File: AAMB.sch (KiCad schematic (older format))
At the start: 6 parts, among them J1 Screw_Terminal_01x04, J2 PJRAS4X2U01X, J3 SPKR L, J4 SPKR R, J5 Screw_Terminal_01x03

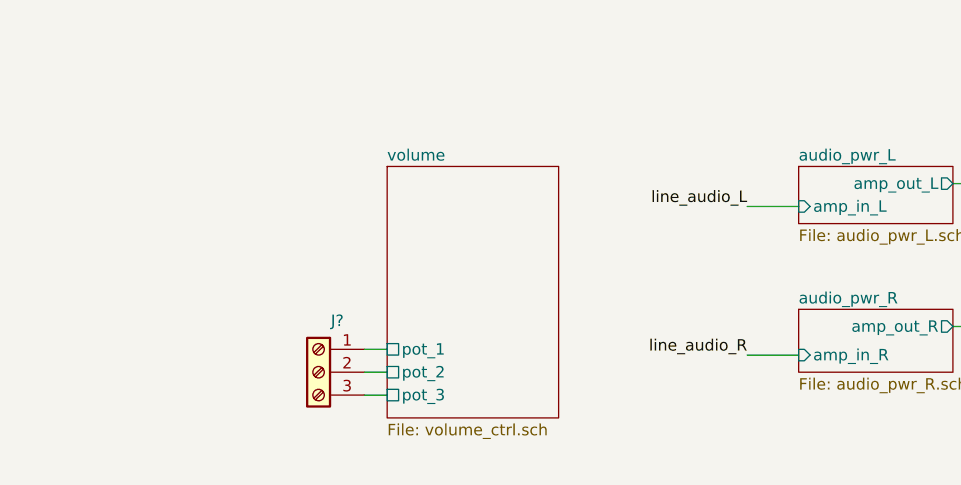
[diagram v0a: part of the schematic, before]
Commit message: Volume circuit placed and connected. Page titles added.
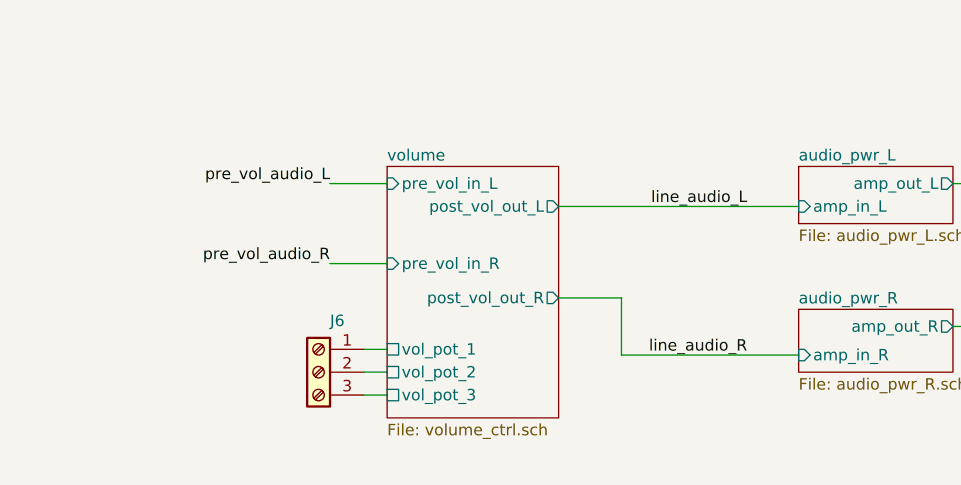
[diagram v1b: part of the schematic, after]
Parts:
- gave numbers to parts that had none: 1
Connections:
- net labels added: pre_vol_audio_L, pre_vol_audio_R
- wire segments 37 -> 41
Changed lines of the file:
@@
 encoding utf-8
 Sheet 1 5
-Title ""
-Date ""
-Rev ""
-Comp ""
-Comment1 ""
-Comment2 ""
+Title "Audio Amp Main Board Top"
+Date "2020-01-21"
+Rev "A"
+Comp "Shawn Adams"
+Comment1 "Based on designs by Elliot Sound Products"
+Comment2 "https://sound-au.com/"
 Comment3 ""
 Comment4 ""
@@
 Wire Wire Line
 	900  1550 1100 1550
-Wire Wire Line
-	6925 4275 7150 4275
 NoConn ~ 1050 4925
 NoConn ~ 1050 4425
@@
 line_audio_R
 Wire Wire Line
-	7150 4925 6925 4925
-Wire Wire Line
 	8450 4325 8450 4800
 Text Label 7950 4800 0    50   ~ 0
@@
 	7825 4800 8450 4800
 $Comp
-L Connector:Screw_Terminal_01x03 J?
+L Connector:Screw_Terminal_01x03 J6
 U 1 1 5E22654E
 P 5050 5000
-F 0 "J?" H 4968 5225 50  0000 C CNN
+F 0 "J6" H 4968 5225 50  0000 C CNN
 F 1 "Screw_Terminal_01x03" H 4968 5226 50  0001 C CNN
 F 2 "" H 5050 5000 50  0001 C CNN
@@
 F0 "volume" 50
 F1 "volume_ctrl.sch" 50
-F2 "pot_1" U L 5350 4900 50
-F3 "pot_2" U L 5350 5000 50
-F4 "pot_3" U L 5350 5100 50
+F2 "vol_pot_1" U L 5350 4900 50
+F3 "vol_pot_2" U L 5350 5000 50
+F4 "vol_pot_3" U L 5350 5100 50
+F5 "post_vol_out_L" O R 6100 4275 50
+F6 "pre_vol_in_L" I L 5350 4175 50
+F7 "pre_vol_in_R" I L 5350 4525 50
+F8 "post_vol_out_R" O R 6100 4675 50
 $EndSheet
 Wire Wire Line
@@
 EndData
 $EndBitmap
+Wire Wire Line
+	6100 4675 6375 4675
+Wire Wire Line
+	6375 4675 6375 4925
+Wire Wire Line
+	6375 4925 7150 4925
+Wire Wire Line
+	6100 4275 7150 4275
+Wire Wire Line
+	5350 4175 5100 4175
+Wire Wire Line
+	5350 4525 5100 4525
+Text Label 5100 4175 2    50   ~ 0
+pre_vol_audio_L
+Text Label 5100 4525 2    50   ~ 0
+pre_vol_audio_R
 $EndSCHEMATC

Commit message: Started input select circuit.
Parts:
- added J?: Conn_01x05, symbol Connector_Generic:Conn_01x05
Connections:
- net labels removed: IN1_L, IN1_R, IN2_L, IN2_R, IN3_L, IN3_R, IN4_L, IN4_R
- wire segments 41 -> 60
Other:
- note added: "volume knob\n10k linear pot"
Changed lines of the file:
@@
 $Descr A4 11693 8268
 encoding utf-8
-Sheet 1 5
+Sheet 1 6
 Title "Audio Amp Main Board Top"
 Date "2020-01-21"
 Rev "A"
 Comp "Shawn Adams"
-Comment1 "Based on designs by Elliot Sound Products"
-Comment2 "https://sound-au.com/"
+Comment1 "https://sound-au.com/"
+Comment2 "Based on designs by Elliot Sound Products"
 Comment3 ""
 Comment4 ""
@@
 Wire Wire Line
 	925  1800 925  1650
-Text Label 1150 3275 0    50   ~ 0
-IN1_R
-Text Label 1150 3075 0    50   ~ 0
-IN1_L
 Text Label 6925 4275 2    50   ~ 0
 line_audio_L
@@
 	1    0    0    -1
 $EndComp
-Wire Wire Line
-	1050 3775 1150 3775
-Text Label 1150 3775 0    50   ~ 0
-IN2_R
-Text Label 1150 3575 0    50   ~ 0
-IN2_L
-Wire Wire Line
-	1050 4075 1150 4075
-Wire Wire Line
-	1050 4275 1150 4275
-Text Label 1150 4275 0    50   ~ 0
-IN3_R
-Text Label 1150 4075 0    50   ~ 0
-IN3_L
-Wire Wire Line
-	1050 4575 1150 4575
-Wire Wire Line
-	1050 4775 1150 4775
-Text Label 1150 4775 0    50   ~ 0
-IN4_R
-Text Label 1150 4575 0    50   ~ 0
-IN4_L
 $Comp
 L power:GND #PWR01
@@
 	850  625  725  625
 Wire Wire Line
-	1150 3575 1050 3575
-Wire Wire Line
-	1150 3275 1050 3275
-Wire Wire Line
-	1150 3075 1050 3075
+	1175 3575 1050 3575
+Wire Wire Line
+	1100 3275 1050 3275
 Wire Wire Line
 	900  1450 950  1450
@@
 U 1 1 5E3F968D
 P 10000 4500
-F 0 "J3" H 10080 4492 50  0000 L CNN
-F 1 "SPKR L" H 10080 4401 50  0000 L CNN
+F 0 "J3" H 10075 4400 50  0000 L CNN
+F 1 "SPKR L" H 10075 4500 50  0000 L CNN
 F 2 "TerminalBlock_Phoenix:TerminalBlock_Phoenix_MKDS-1,5-2_1x02_P5.00mm_Horizontal" H 10000 4500 50  0001 C CNN
 F 3 "https://www.digikey.com/product-detail/en/phoenix-contact/1715022/277-1258-ND/260626" H 10000 4500 50  0001 C CNN
@@
 U 1 1 5E3FA9B2
 P 10000 4750
-F 0 "J4" H 10080 4742 50  0000 L CNN
-F 1 "SPKR R" H 10080 4651 50  0000 L CNN
+F 0 "J4" H 10075 4650 50  0000 L CNN
+F 1 "SPKR R" H 10075 4750 50  0000 L CNN
 F 2 "TerminalBlock_Phoenix:TerminalBlock_Phoenix_MKDS-1,5-2_1x02_P5.00mm_Horizontal" H 10000 4750 50  0001 C CNN
 F 3 "https://www.digikey.com/product-detail/en/phoenix-contact/1715022/277-1258-ND/260626" H 10000 4750 50  0001 C CNN
@@
 Text Label 5100 4525 2    50   ~ 0
 pre_vol_audio_R
+Text Notes 4175 5150 0    50   ~ 0
+volume knob\n10k linear pot
+$Sheet
+S 2100 2950 1175 1625
+U 5E487042
+F0 "input_select" 50
+F1 "input_select.sch" 50
+F2 "IN1_L" I L 2100 3075 50
+F3 "IN1_R" I L 2100 3175 50
+F4 "IN2_L" I L 2100 3325 50
+F5 "IN2_R" I L 2100 3425 50
+F6 "IN3_L" I L 2100 3550 50
+F7 "IN3_R" I L 2100 3650 50
+F8 "IN4_L" I L 2100 3775 50
+F9 "IN4_R" I L 2100 3875 50
+F10 "input_sw_0" I L 2100 4075 50
+F11 "input_sw_1" I L 2100 4175 50
+F12 "input_sw_2" I L 2100 4275 50
+F13 "input_sw_3" I L 2100 4375 50
+F14 "input_sw_com" O L 2100 4475 50
+F15 "post_sw_audio_L" O R 3275 3250 50
+F16 "post_sw_audio_R" O R 3275 3475 50
+$EndSheet
+$Comp
+L Connector_Generic:Conn_01x05 J?
+U 1 1 5E5AF883
+P 1800 4275
+F 0 "J?" H 1725 4000 50  0000 C CNN
+F 1 "Conn_01x05" H 1718 4601 50  0001 C CNN
+F 2 "" H 1800 4275 50  0001 C CNN
+F 3 "~" H 1800 4275 50  0001 C CNN
+	1    1800 4275
+	-1   0    0    -1
+$EndComp
+Wire Wire Line
+	2000 4075 2100 4075
+Wire Wire Line
+	2000 4175 2100 4175
+Wire Wire Line
+	2000 4275 2100 4275
+Wire Wire Line
+	2000 4375 2100 4375
+Wire Wire Line
+	2000 4475 2100 4475
+Wire Wire Line
+	1050 3075 2100 3075
+Wire Wire Line
+	2100 3175 1100 3175
+Wire Wire Line
+	1100 3175 1100 3275
+Wire Wire Line
+	1175 3575 1175 3325
+Wire Wire Line
+	1175 3325 2100 3325
+Wire Wire Line
+	1250 3775 1250 3425
+Wire Wire Line
+	1250 3425 2100 3425
+Wire Wire Line
+	1050 3775 1250 3775
+Wire Wire Line
+	1350 4075 1350 3550
+Wire Wire Line
+	1350 3550 2100 3550
+Wire Wire Line
+	1050 4075 1350 4075
+Wire Wire Line
+	1425 4275 1425 3650
+Wire Wire Line
+	1425 3650 2100 3650
+Wire Wire Line
+	1050 4275 1425 4275
+Wire Wire Line
+	1525 4575 1525 3775
+Wire Wire Line
+	1525 3775 2100 3775
+Wire Wire Line
+	1050 4575 1525 4575
+Wire Wire Line
+	1600 4775 1600 3875
+Wire Wire Line
+	1600 3875 2100 3875
+Wire Wire Line
+	1050 4775 1600 4775
 $EndSCHEMATC

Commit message: Opened on home office computer. Some rescue and lib conversion happened. Need to confirm no changes on work laptop.
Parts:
- J2: symbol Connectors-amp:PJRAS4X2U01X -> AAMB-rescue:PJRAS4X2U01X-Connectors-amp
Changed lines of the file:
@@
 EESchema Schematic File Version 4
-LIBS:AAMB-cache
 EELAYER 30 0
 EELAYER END
@@
 line_audio_L
 $Comp
-L Connectors-amp:PJRAS4X2U01X J2
+L AAMB-rescue:PJRAS4X2U01X-Connectors-amp J2
 U 1 1 5E2F4D8A
 P 900 3325
@@
 $EndComp
 $Comp
-L Connectors-amp:PJRAS4X2U01X J2
+L AAMB-rescue:PJRAS4X2U01X-Connectors-amp J2
 U 2 1 5E2F72BC
 P 900 3825
@@
 $EndComp
 $Comp
-L Connectors-amp:PJRAS4X2U01X J2
+L AAMB-rescue:PJRAS4X2U01X-Connectors-amp J2
 U 3 1 5E2F87B8
 P 900 4325
@@
 $EndComp
 $Comp
-L Connectors-amp:PJRAS4X2U01X J2
+L AAMB-rescue:PJRAS4X2U01X-Connectors-amp J2
 U 4 1 5E2FA23A
 P 900 4825
@@
 	8675 4325 8450 4325
 $Comp
-L Power-amp:+35V #PWR0106
+L AAMB-rescue:+35V-Power-amp #PWR0106
 U 1 1 5E1EC4AA
 P 1100 1550
@@
 $EndComp
 $Comp
-L Power-amp:-35V #PWR0107
+L AAMB-rescue:-35V-Power-amp #PWR0107
 U 1 1 5E1EDDCB
 P 1100 1750
@@
 $EndComp
 $Comp
-L Power-amp:+35V #PWR0112
+L AAMB-rescue:+35V-Power-amp #PWR0112
 U 1 1 5E239287
 P 725 625
@@
 $EndComp
 $Comp
-L Power-amp:-35V #PWR0113
+L AAMB-rescue:-35V-Power-amp #PWR0113
 U 1 1 5E2397FB
 P 975 600

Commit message: Fixed several DRC errors. Tied audoi input returns to GND. Added Switch logic.
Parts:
- removed J?: Conn_01x05, symbol Connector_Generic:Conn_01x05
- added J7: Conn_01x04, symbol Connector_Generic:Conn_01x04
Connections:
- wire segments 60 -> 72
- no-connect marks 4 -> 0
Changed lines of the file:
@@
 EESchema Schematic File Version 4
+LIBS:AAMB-cache
 EELAYER 30 0
 EELAYER END
@@
 Comment4 ""
 $EndDescr
-$Comp
-L power:PWR_FLAG #FLG01
-U 1 1 5A7AA76B
-P 575 600
-F 0 "#FLG01" H 575 675 50  0001 C CNN
-F 1 "PWR_FLAG" H 575 774 50  0001 C CNN
-F 2 "" H 575 600 50  0001 C CNN
-F 3 "~" H 575 600 50  0001 C CNN
-	1    575  600
-	1    0    0    -1
-$EndComp
 $Sheet
 S 7150 4100 675  250
@@
 F3 "amp_out_L" O R 7825 4175 50
 $EndSheet
-$Comp
-L power:GND #PWR0105
-U 1 1 5E2D317B
-P 925 1800
-F 0 "#PWR0105" H 925 1550 50  0001 C CNN
-F 1 "GND" H 930 1627 50  0000 C CNN
-F 2 "" H 925 1800 50  0001 C CNN
-F 3 "" H 925 1800 50  0001 C CNN
-	1    925  1800
-	1    0    0    -1
-$EndComp
 Wire Wire Line
 	900  1650 925  1650
@@
 	1    0    0    -1
 $EndComp
-$Comp
-L power:GND #PWR01
-U 1 1 5A837871
-P 575 600
-F 0 "#PWR01" H 575 350 50  0001 C CNN
-F 1 "GND" H 580 427 50  0000 C CNN
-F 2 "" H 575 600 50  0001 C CNN
-F 3 "" H 575 600 50  0001 C CNN
-	1    575  600
-	1    0    0    -1
-$EndComp
 Wire Wire Line
 	8675 4325 8450 4325
@@
 Wire Wire Line
 	900  1550 1100 1550
-NoConn ~ 1050 4925
-NoConn ~ 1050 4425
-NoConn ~ 1050 3925
-NoConn ~ 1050 3425
 $Comp
 L power:PWR_FLAG #FLG0101
 U 1 1 5E238666
-P 850 625
-F 0 "#FLG0101" H 850 700 50  0001 C CNN
-F 1 "PWR_FLAG" H 850 799 50  0001 C CNN
-F 2 "" H 850 625 50  0001 C CNN
-F 3 "~" H 850 625 50  0001 C CNN
-	1    850  625
+P 700 625
+F 0 "#FLG0101" H 700 700 50  0001 C CNN
+F 1 "PWR_FLAG" H 700 799 50  0001 C CNN
+F 2 "" H 700 625 50  0001 C CNN
+F 3 "~" H 700 625 50  0001 C CNN
+	1    700  625
 	1    0    0    -1
 $EndComp
@@
 L power:PWR_FLAG #FLG0102
 U 1 1 5E238B4D
-P 975 600
-F 0 "#FLG0102" H 975 675 50  0001 C CNN
-F 1 "PWR_FLAG" H 975 774 50  0001 C CNN
-F 2 "" H 975 600 50  0001 C CNN
-F 3 "~" H 975 600 50  0001 C CNN
-	1    975  600
-	1    0    0    -1
-$EndComp
-$Comp
-L AAMB-rescue:+35V-Power-amp #PWR0112
-U 1 1 5E239287
-P 725 625
-F 0 "#PWR0112" H 900 450 50  0001 C CNN
-F 1 "+35V" H 725 725 39  0000 C CNN
-F 2 "" H 725 625 50  0001 C CNN
-F 3 "" H 725 625 50  0001 C CNN
-	1    725  625
+P 825 600
+F 0 "#FLG0102" H 825 675 50  0001 C CNN
+F 1 "PWR_FLAG" H 825 774 50  0001 C CNN
+F 2 "" H 825 600 50  0001 C CNN
+F 3 "~" H 825 600 50  0001 C CNN
+	1    825  600
 	1    0    0    -1
 $EndComp
@@
 L AAMB-rescue:-35V-Power-amp #PWR0113
 U 1 1 5E2397FB
-P 975 600
-F 0 "#PWR0113" H 1150 425 50  0001 C CNN
-F 1 "-35V" H 1025 500 39  0000 C CNN
-F 2 "" H 975 600 50  0001 C CNN
-F 3 "" H 975 600 50  0001 C CNN
-	1    975  600
-	1    0    0    -1
-$EndComp
-Wire Wire Line
-	850  625  725  625
+P 825 600
+F 0 "#PWR0113" H 1000 425 50  0001 C CNN
+F 1 "-35V" H 875 500 39  0000 C CNN
+F 2 "" H 825 600 50  0001 C CNN
+F 3 "" H 825 600 50  0001 C CNN
+	1    825  600
+	1    0    0    -1
+$EndComp
+Wire Wire Line
+	700  625  575  625
 Wire Wire Line
 	1175 3575 1050 3575
@@
 F 3 "https://www.digikey.com/product-detail/en/phoenix-contact/1715022/277-1258-ND/260626" H 10000 4750 50  0001 C CNN
 	1    10000 4750
-	1    0    0    -1
-$EndComp
-$Comp
-L power:GND #PWR07
-U 1 1 5E3FE2D7
-P 9700 4925
-F 0 "#PWR07" H 9700 4675 50  0001 C CNN
-F 1 "GND" H 9705 4752 50  0000 C CNN
-F 2 "" H 9700 4925 50  0001 C CNN
-F 3 "" H 9700 4925 50  0001 C CNN
-	1    9700 4925
 	1    0    0    -1
 $EndComp
@@
 Wire Wire Line
 	9800 4750 9450 4750
-Wire Wire Line
-	9800 4850 9700 4850
-Wire Wire Line
-	9700 4850 9700 4925
-Wire Wire Line
-	9800 4600 9700 4600
-Wire Wire Line
-	9700 4600 9700 4850
-Connection ~ 9700 4850
 $Comp
 L Connector:Screw_Terminal_01x03 J5
@@
 Wire Wire Line
 	6100 4275 7150 4275
-Wire Wire Line
-	5350 4175 5100 4175
-Wire Wire Line
-	5350 4525 5100 4525
 Text Label 5100 4175 2    50   ~ 0
 pre_vol_audio_L
@@
 F8 "IN4_L" I L 2100 3775 50
 F9 "IN4_R" I L 2100 3875 50
-F10 "input_sw_0" I L 2100 4075 50
-F11 "input_sw_1" I L 2100 4175 50
-F12 "input_sw_2" I L 2100 4275 50
-F13 "input_sw_3" I L 2100 4375 50
-F14 "input_sw_com" O L 2100 4475 50
-F15 "post_sw_audio_L" O R 3275 3250 50
-F16 "post_sw_audio_R" O R 3275 3475 50
+F10 "input_sw_1" I L 2100 4175 50
+F11 "input_sw_2" I L 2100 4275 50
+F12 "input_sw_3" I L 2100 4375 50
+F13 "input_sw_com" O L 2100 4475 50
+F14 "post_sw_audio_L" O R 3275 3250 50
+F15 "post_sw_audio_R" O R 3275 3475 50
 $EndSheet
-$Comp
-L Connector_Generic:Conn_01x05 J?
-U 1 1 5E5AF883
+Wire Wire Line
+	2000 4175 2100 4175
+Wire Wire Line
+	2000 4275 2100 4275
+Wire Wire Line
+	2000 4375 2100 4375
+Wire Wire Line
+	2000 4475 2100 4475
+Wire Wire Line
+	1050 3075 2100 3075
+Wire Wire Line
+	2100 3175 1100 3175
+Wire Wire Line
+	1100 3175 1100 3275
+Wire Wire Line
+	1175 3575 1175 3325
+Wire Wire Line
+	1175 3325 2100 3325
+Wire Wire Line
+	1250 3775 1250 3425
+Wire Wire Line
+	1250 3425 2100 3425
+Wire Wire Line
+	1050 3775 1250 3775
+Wire Wire Line
+	1350 4075 1350 3550
+Wire Wire Line
+	1350 3550 2100 3550
+Wire Wire Line
+	1050 4075 1350 4075
+Wire Wire Line
+	1425 4275 1425 3650
+Wire Wire Line
+	1425 3650 2100 3650
+Wire Wire Line
+	1050 4275 1425 4275
+Wire Wire Line
+	1525 4575 1525 3775
+Wire Wire Line
+	1525 3775 2100 3775
+Wire Wire Line
+	1050 4575 1525 4575
+Wire Wire Line
+	1600 4775 1600 3875
+Wire Wire Line
+	1600 3875 2100 3875
+Wire Wire Line
+	1050 4775 1600 4775
+$Comp
+L AAMB-rescue:+35V-Power-amp #PWR0112
+U 1 1 5E239287
+P 575 625
+F 0 "#PWR0112" H 750 450 50  0001 C CNN
+F 1 "+35V" H 575 725 39  0000 C CNN
+F 2 "" H 575 625 50  0001 C CNN
+F 3 "" H 575 625 50  0001 C CNN
+	1    575  625
+	1    0    0    -1
+$EndComp
+$Comp
+L Connector_Generic:Conn_01x04 J7
+U 1 1 5E2AFFDD
 P 1800 4275
-F 0 "J?" H 1725 4000 50  0000 C CNN
-F 1 "Conn_01x05" H 1718 4601 50  0001 C CNN
+F 0 "J7" H 1718 4500 50  0000 C CNN
+F 1 "Conn_01x04" H 1718 4501 50  0001 C CNN
 F 2 "" H 1800 4275 50  0001 C CNN
 F 3 "~" H 1800 4275 50  0001 C CNN
@@
 	-1   0    0    -1
 $EndComp
-Wire Wire Line
-	2000 4075 2100 4075
-Wire Wire Line
-	2000 4175 2100 4175
-Wire Wire Line
-	2000 4275 2100 4275
-Wire Wire Line
-	2000 4375 2100 4375
-Wire Wire Line
-	2000 4475 2100 4475
-Wire Wire Line
-	1050 3075 2100 3075
-Wire Wire Line
-	2100 3175 1100 3175
-Wire Wire Line
-	1100 3175 1100 3275
-Wire Wire Line
-	1175 3575 1175 3325
-Wire Wire Line
-	1175 3325 2100 3325
-Wire Wire Line
-	1250 3775 1250 3425
-Wire Wire Line
-	1250 3425 2100 3425
-Wire Wire Line
-	1050 3775 1250 3775
-Wire Wire Line
-	1350 4075 1350 3550
-Wire Wire Line
-	1350 3550 2100 3550
-Wire Wire Line
-	1050 4075 1350 4075
-Wire Wire Line
-	1425 4275 1425 3650
-Wire Wire Line
-	1425 3650 2100 3650
-Wire Wire Line
-	1050 4275 1425 4275
-Wire Wire Line
-	1525 4575 1525 3775
-Wire Wire Line
-	1525 3775 2100 3775
-Wire Wire Line
-	1050 4575 1525 4575
-Wire Wire Line
-	1600 4775 1600 3875
-Wire Wire Line
-	1600 3875 2100 3875
-Wire Wire Line
-	1050 4775 1600 4775
+$Comp
+L power:PWR_FLAG #FLG0103
+U 1 1 5E2EA3BE
+P 1150 700
+F 0 "#FLG0103" H 1150 775 50  0001 C CNN
+F 1 "PWR_FLAG" H 1150 874 50  0001 C CNN
+F 2 "" H 1150 700 50  0001 C CNN
+F 3 "~" H 1150 700 50  0001 C CNN
+	1    1150 700
+	1    0    0    -1
+$EndComp
+$Comp
+L power:PWR_FLAG #FLG0104
+U 1 1 5E2EA3C4
+P 1275 600
+F 0 "#FLG0104" H 1275 675 50  0001 C CNN
+F 1 "PWR_FLAG" H 1275 774 50  0001 C CNN
+F 2 "" H 1275 600 50  0001 C CNN
+F 3 "~" H 1275 600 50  0001 C CNN
+	1    1275 600
+	1    0    0    -1
+$EndComp
+Wire Wire Line
+	1150 700  1025 700
+$Comp
+L power:-12V #PWR0115
+U 1 1 5E2EE74B
+P 1275 600
+F 0 "#PWR0115" H 1275 700 50  0001 C CNN
+F 1 "-12V" H 1290 773 50  0000 C CNN
+F 2 "" H 1275 600 50  0001 C CNN
+F 3 "" H 1275 600 50  0001 C CNN
+	1    1275 600
+	-1   0    0    1
+$EndComp
+$Comp
+L power:+12V #PWR0116
+U 1 1 5E2EF2D1
+P 1025 700
+F 0 "#PWR0116" H 1025 550 50  0001 C CNN
+F 1 "+12V" H 1040 873 50  0000 C CNN
+F 2 "" H 1025 700 50  0001 C CNN
+F 3 "" H 1025 700 50  0001 C CNN
+	1    1025 700
+	1    0    0    -1
+$EndComp
+Wire Wire Line
+	3275 3250 4250 3250
+Wire Wire Line
+	4250 3250 4250 4175
+Wire Wire Line
+	4250 4175 5350 4175
+Wire Wire Line
+	3275 3475 4100 3475
+Wire Wire Line
+	4100 3475 4100 4525
+Wire Wire Line
+	4100 4525 5350 4525
+$Comp
+L power:GND #PWR0105
+U 1 1 5E32ADD9
+P 925 1800
+F 0 "#PWR0105" H 925 1550 50  0001 C CNN
+F 1 "GND" H 925 1650 50  0001 C CNN
+F 2 "" H 925 1800 50  0001 C CNN
+F 3 "" H 925 1800 50  0001 C CNN
+	1    925  1800
+	1    0    0    -1
+$EndComp
+$Comp
+L power:GND #PWR0118
+U 1 1 5E33EF10
+P 9675 4925
+F 0 "#PWR0118" H 9675 4675 50  0001 C CNN
+F 1 "GND" H 9675 4775 50  0001 C CNN
+F 2 "" H 9675 4925 50  0001 C CNN
+F 3 "" H 9675 4925 50  0001 C CNN
+	1    9675 4925
+	1    0    0    -1
+$EndComp
+Wire Wire Line
+	9675 4925 9675 4850
+Wire Wire Line
+	9675 4600 9800 4600
+Wire Wire Line
+	9800 4850 9675 4850
+Connection ~ 9675 4850
+Wire Wire Line
+	9675 4850 9675 4600
+$Comp
+L power:PWR_FLAG #FLG0105
+U 1 1 5E362BB1
+P 1475 600
+F 0 "#FLG0105" H 1475 675 50  0001 C CNN
+F 1 "PWR_FLAG" H 1475 774 50  0001 C CNN
+F 2 "" H 1475 600 50  0001 C CNN
+F 3 "~" H 1475 600 50  0001 C CNN
+	1    1475 600
+	1    0    0    -1
+$EndComp
+$Comp
+L power:GND #PWR0121
+U 1 1 5E36386F
+P 1475 600
+F 0 "#PWR0121" H 1475 350 50  0001 C CNN
+F 1 "GND" H 1475 450 50  0001 C CNN
+F 2 "" H 1475 600 50  0001 C CNN
+F 3 "" H 1475 600 50  0001 C CNN
+	1    1475 600
+	1    0    0    -1
+$EndComp
+$Comp
+L power:GND #PWR01
+U 1 1 5E399DE3
+P 1100 5000
+F 0 "#PWR01" H 1100 4750 50  0001 C CNN
+F 1 "GND" H 1100 4850 50  0001 C CNN
+F 2 "" H 1100 5000 50  0001 C CNN
+F 3 "" H 1100 5000 50  0001 C CNN
+	1    1100 5000
+	1    0    0    -1
+$EndComp
+Wire Wire Line
+	1100 5000 1100 4925
+Wire Wire Line
+	1100 3425 1050 3425
+Wire Wire Line
+	1050 3925 1100 3925
+Connection ~ 1100 3925
+Wire Wire Line
+	1100 3925 1100 3425
+Wire Wire Line
+	1050 4425 1100 4425
+Connection ~ 1100 4425
+Wire Wire Line
+	1100 4425 1100 3925
+Wire Wire Line
+	1050 4925 1100 4925
+Connection ~ 1100 4925
+Wire Wire Line
+	1100 4925 1100 4425
 $EndSCHEMATC

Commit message: Schecmatic cleanup.
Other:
- moved on the sheet: J2A, J2B, J2C, J2D, J3, J4, J5, J6, J7
